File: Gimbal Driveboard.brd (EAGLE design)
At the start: 68.6 x 58.7 mm, 23 parts, among them J2 APP_2POS_CONFIG12V_HORIZ, U1 OKI-78SR-5/1.5-W36HC, U2 MAX232D, U3 MAX232D

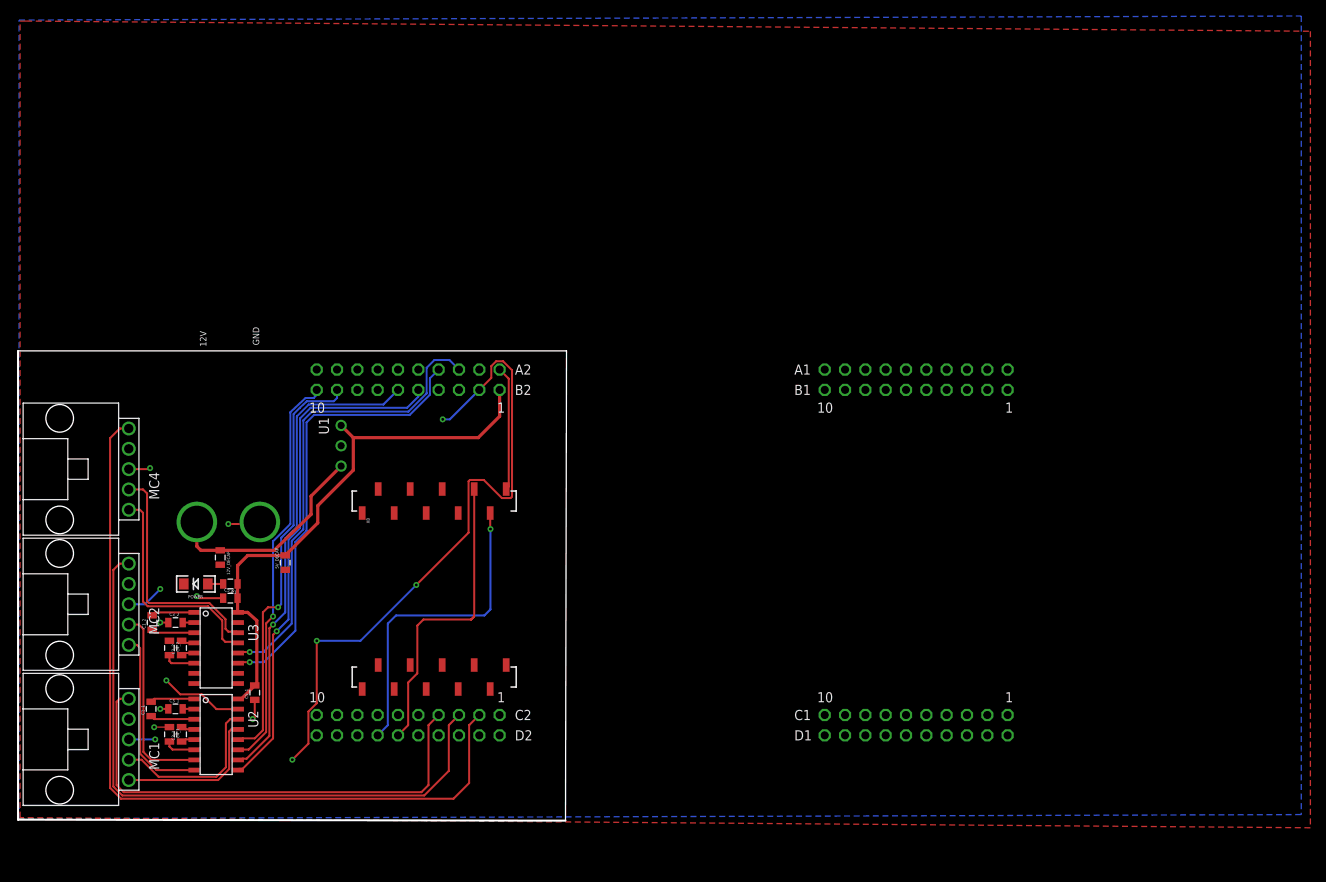
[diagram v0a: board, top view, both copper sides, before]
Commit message: Remade schematic to avoid physical interference with ethernet port
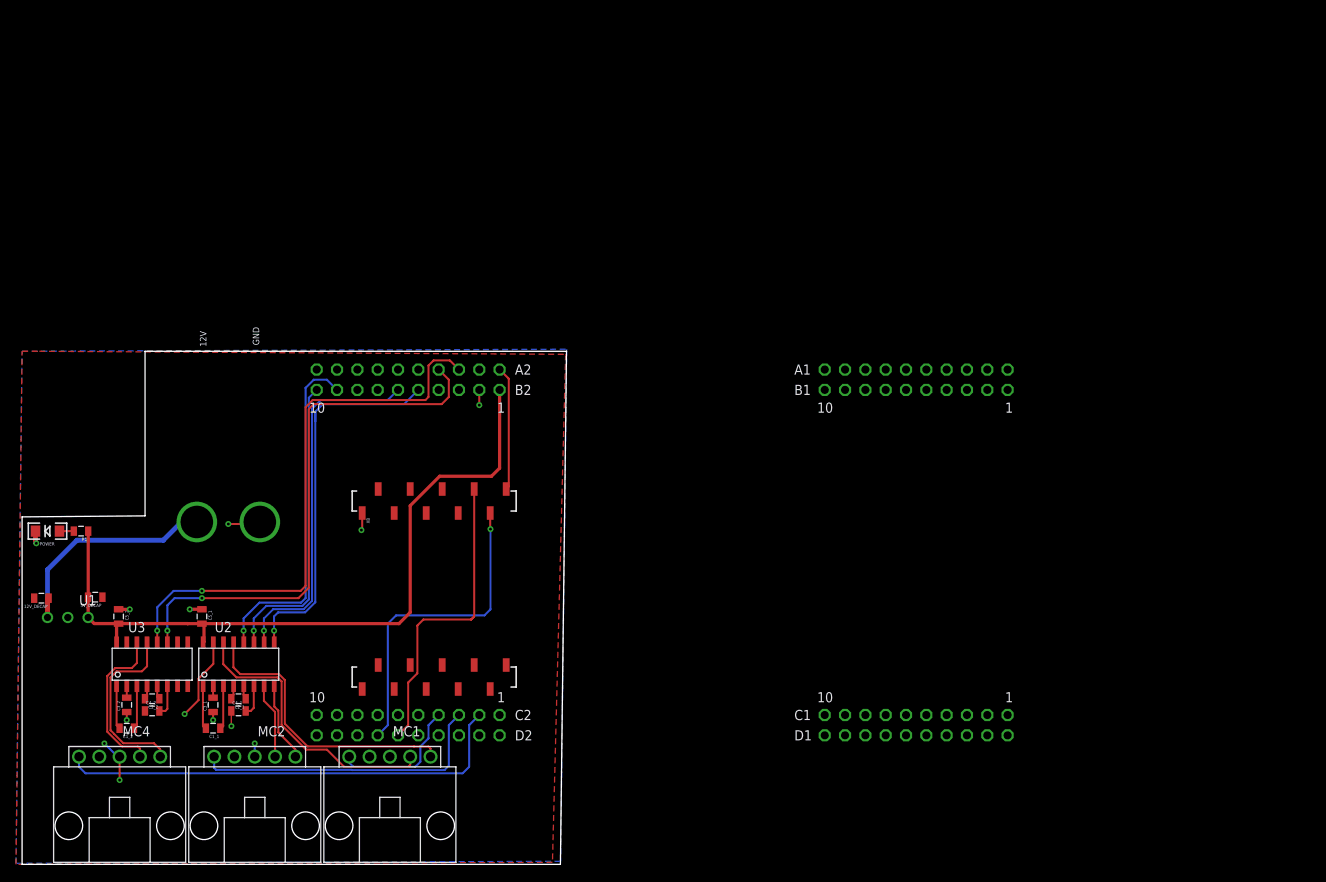
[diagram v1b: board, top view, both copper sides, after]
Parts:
- moved U1 41.3 mm to (3.68, 25.3), turned to 180 degrees
- moved MC4 36.0 mm to (12.7, 7.87), turned to 180 degrees
- moved MC1 32.7 mm to (46.5, 7.87), turned to 180 degrees
- moved MC2 24.7 mm to (29.6, 7.87), turned to 180 degrees
- moved 5V_DECAP 24.1 mm to (9.65, 27.8), turned to 180 degrees
- moved 12V_DECAP 22.9 mm to (2.92, 27.7), turned to 180 degrees
- moved R1 19.8 mm to (7.87, 36.1)
- moved POWER 19.7 mm to (3.68, 36.1)
- moved C5_2 14.2 mm to (12.6, 25.4), turned to 270 degrees
- moved C1_2 13.6 mm to (13.6, 11.4), turned to 180 degrees
- moved C3_2 12.0 mm to (13.6, 14.4), turned to 90 degrees
- moved C5_1 11.6 mm to (23.0, 25.4), turned to 270 degrees
- moved U2 9.23 mm to (27.6, 19.4), turned to 0 degrees
- moved C4_1 9.12 mm to (27.6, 13.6), turned to 0 degrees
- moved C2_1 8.39 mm to (27.6, 15.1), turned to 180 degrees
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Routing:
- net GND: track 117.5 -> 34.1 mm, vias 14 -> 13
- net PWM_1: track 61.1 -> 16.9 mm
- net PWM_3: track 101.8 -> 57.7 mm
- net PWM_2: track 80.5 -> 37.9 mm
- net +5V: track 70.2 -> 94.1 mm
- net N$37: track 19.0 -> 36.2 mm
- net RX_2: track 64.9 -> 48.9 mm
- net N$36: track 20.7 -> 35.7 mm
- net N$35: track 24.8 -> 9.97 mm
- net TX_2: track 60.6 -> 45.9 mm
- net TX_1: track 50.5 -> 37.5 mm
- net N$34: track 22.4 -> 9.95 mm
- net TX_3: track 55.9 -> 67.7 mm, vias 1 -> 2
- net RX_3: track 59.3 -> 70.8 mm, vias 1 -> 2
- net N$32: track 29.6 -> 19.9 mm
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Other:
- board size 68.6 x 58.7 mm -> 68.1 x 64.1 mm

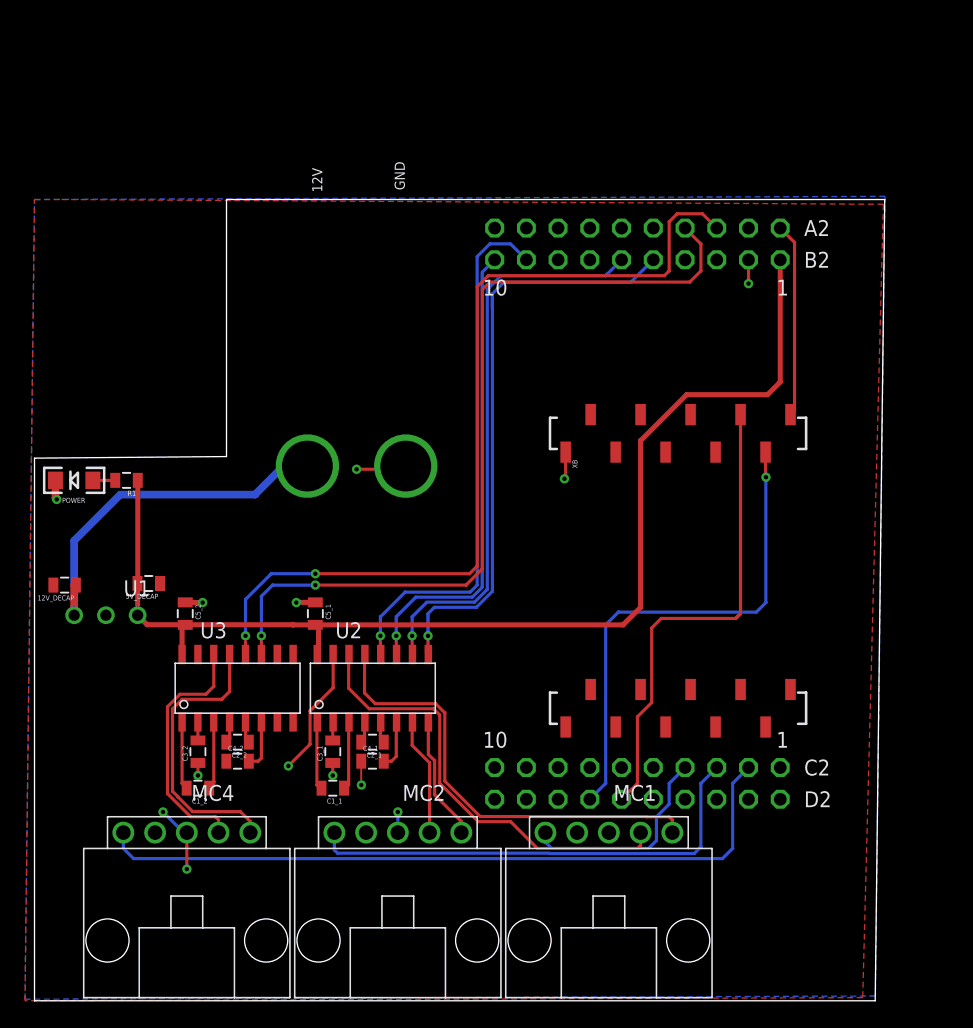
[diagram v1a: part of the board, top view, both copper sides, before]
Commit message: Updated schematic and board for final board review
added I2C Molex SL4
Added mounting tab and holes
cleaned up lines and traces
Added signature and board information
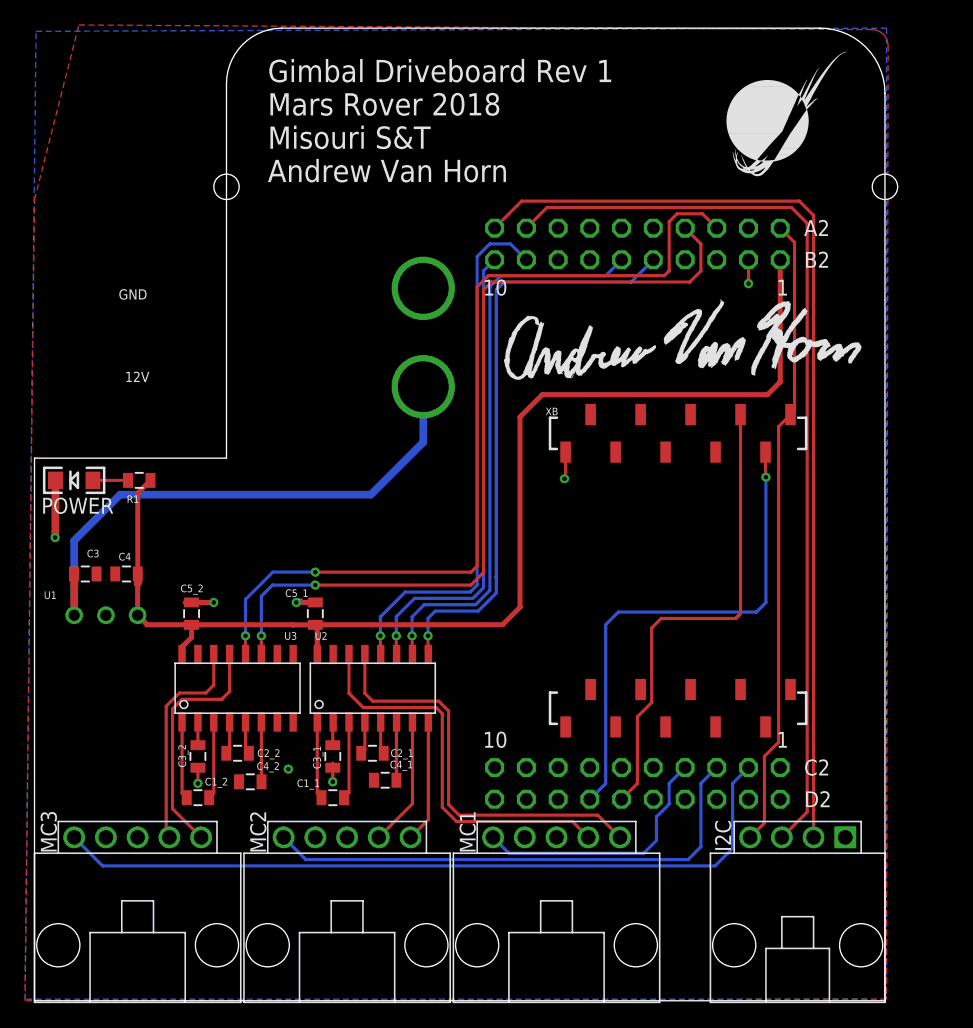
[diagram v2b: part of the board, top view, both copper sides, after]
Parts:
- removed 12V_DECAP, 5V_DECAP: 10uF, SparkFun-Capacitors:0805
- removed MC4: SL05, MRDT-Connectors:MOLEX_SL_05_TH
- added C3, C4: 10uF, SparkFun-Capacitors:0805
- added I2C: SL04, MRDT-Connectors:MOLEX_SL_04_TH
- added LOGO1: MRDT_LOGO, MRDT-Hardware:MRDT_LOGO
- added MC3: SL05, MRDT-Connectors:MOLEX_SL_05_TH
- added U$3: ANDREW_VAN_HORN_SIGNATURE, MRDT-Signatures:ANDREW_VAN_HORN_SIGNATURE
- moved J2 29.8 mm to (3.43, 39.6), turned to 0 degrees
- moved MC1 4.21 mm to (42.3, 7.49)
- moved MC2 4.08 mm to (25.5, 7.49)
- moved C4_2 1.94 mm to (17.8, 11.9)
- moved C4_1 1.83 mm to (28.6, 12.1)
- moved R1 1.02 mm to (8.89, 36.1)
- moved C2_1 0.89 mm to (27.6, 14.2)
- moved C2_2 0.89 mm to (16.8, 14.2)
- moved C1_1 0.76 mm to (24.4, 10.7)
- moved C1_2 0.76 mm to (13.6, 10.7)
- moved C5_2 0.51 mm to (13.1, 25.4)
- moved C3_1 0.38 mm to (24.4, 14.0)
- moved C3_2 0.38 mm to (13.6, 14.0)
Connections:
- new net SCL: I2C.3, U$1.PN5
- new net SDA: I2C.2, U$1.PN4
- net +3V3: now also I2C.4
- net +5V: now also C4.2; no longer 5V_DECAP.2
- net GND: now also C3.2, C4.1, I2C.1, MC3.3; no longer 12V_DECAP.2, 5V_DECAP.1, MC4.3
- net N$32: now also MC3.4; no longer MC4.4
- net N$33: now also MC3.5; no longer MC4.5
- net N$5: now also C3.1; no longer 12V_DECAP.1
- net PWM_3: now also MC3.1; no longer MC4.1
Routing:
- net SDA: track 0.00 -> 76.7 mm
- net SCL: track 0.00 -> 73.7 mm
- net +3V3: track 15.5 -> 50.7 mm
- net GND: track 34.1 -> 15.7 mm, vias 13 -> 8
- net N$5: track 29.7 -> 44.9 mm
- net N$36: track 35.7 -> 31.4 mm
- net PWM_1: track 16.9 -> 20.8 mm
- net PWM_3: track 57.7 -> 61.2 mm
- net PWM_2: track 37.9 -> 41.4 mm
- net N$33: track 22.8 -> 19.3 mm
- net N$37: track 36.2 -> 32.7 mm
- net +5V: track 94.1 -> 96.7 mm
- net N$32: track 19.9 -> 17.6 mm
- net RX_2: track 48.9 -> 47.8 mm
- net N$17: track 1.79 -> 2.81 mm
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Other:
- board size 68.1 x 64.1 mm -> 68.1 x 77.9 mm
- board text added: "Gimbal Driveboard Rev 1 Mars Rover 2018 Misouri S&T Andrew Van Horn"

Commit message: Final board review and Rev 1 Gerbs
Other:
- board size 68.1 x 77.9 mm -> 68.1 x 82.9 mm
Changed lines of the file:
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@@
 <plain>
 <wire x1="0.508" y1="-5.588" x2="68.58" y2="-5.588" width="0" layer="20"/>
-<wire x1="68.58" y1="-5.588" x2="68.58" y2="67.05973125" width="0" layer="20"/>
-<wire x1="68.58" y1="67.05973125" x2="63.37673125" y2="72.263" width="0" layer="20" curve="90"/>
-<wire x1="63.37673125" y1="72.263" x2="20.32" y2="72.263" width="0" layer="20"/>
-<wire x1="20.32" y1="72.263" x2="15.875" y2="67.818" width="0" layer="20" curve="90"/>
-<wire x1="15.875" y1="67.818" x2="15.875" y2="37.846" width="0" layer="20"/>
+<wire x1="68.58" y1="-5.588" x2="68.58" y2="66.560715625" width="0" layer="20"/>
+<wire x1="68.58" y1="66.560715625" x2="57.797715625" y2="77.343" width="0" layer="20" curve="90"/>
+<wire x1="57.797715625" y1="77.343" x2="24.108775" y2="77.343" width="0" layer="20"/>
+<wire x1="24.108775" y1="77.343" x2="15.875" y2="69.109225" width="0" layer="20" curve="90"/>
+<wire x1="15.875" y1="69.109225" x2="15.875" y2="37.846" width="0" layer="20"/>
 <wire x1="15.875" y1="37.846" x2="0.508" y2="37.846" width="0" layer="20"/>
 <wire x1="0.508" y1="37.846" x2="0.508" y2="-5.588" width="0" layer="20"/>
-<hole x="15.875" y="59.563" drill="2.032"/>
-<hole x="68.58" y="59.563" drill="2.032"/>
+<hole x="15.875" y="64.643" drill="2.032"/>
+<hole x="68.58" y="64.643" drill="2.032"/>
 <text x="19.177" y="59.944" size="1.778" layer="25">Gimbal Driveboard Rev 1
 Mars Rover 2018
@@
 <polygon width="0.254" layer="1">
 <vertex x="0.508" y="58.547"/>
-<vertex x="4.064" y="72.517"/>
-<vertex x="67.55731875" y="72.143509375" curve="-89.795916"/>
-<vertex x="68.831909375" y="70.858628125"/>
+<vertex x="3.175" y="78.105"/>
+<vertex x="67.945" y="77.724"/>
 <vertex x="68.707" y="-5.461"/>
 <vertex x="-0.254" y="-5.588"/>
@@
 <via x="24.384" y="11.938" extent="1-16" drill="0.35"/>
 <polygon width="0.254" layer="16">
-<vertex x="0.635" y="72.009"/>
-<vertex x="68.707" y="72.263"/>
+<vertex x="0.127" y="77.851"/>
+<vertex x="68.199" y="78.105"/>
 <vertex x="68.707" y="-5.461"/>
 <vertex x="-0.254" y="-5.461"/>

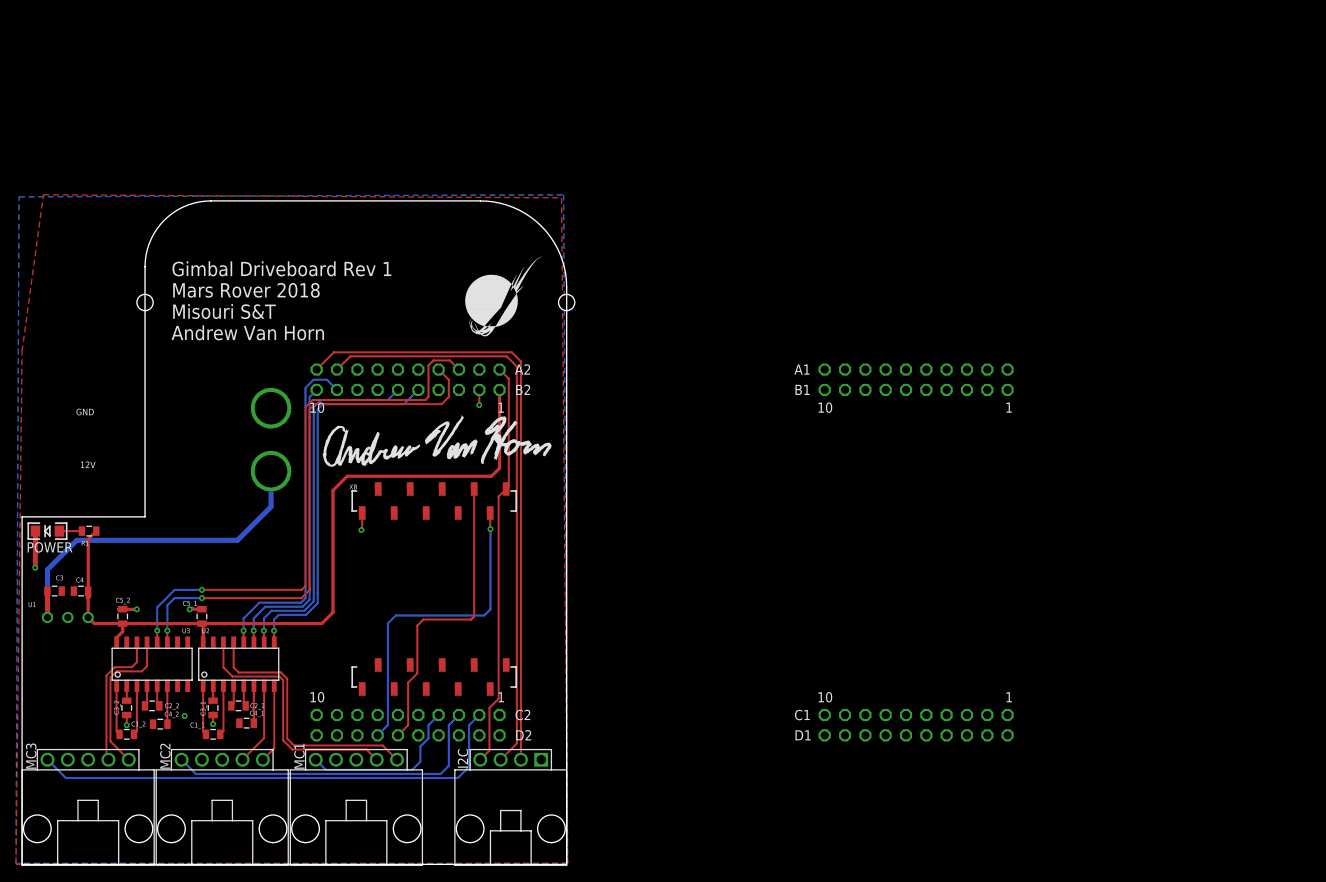
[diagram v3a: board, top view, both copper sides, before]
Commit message: removed TIVA holes on outside of board and rotated silkscreen
I replaced the TIVA package with just the ehaders and re-assigned all the pins in the schematic to match the physical layout on the old package. I rotated the silkscreen 180 so it is oriented right when it is mounted to rover.
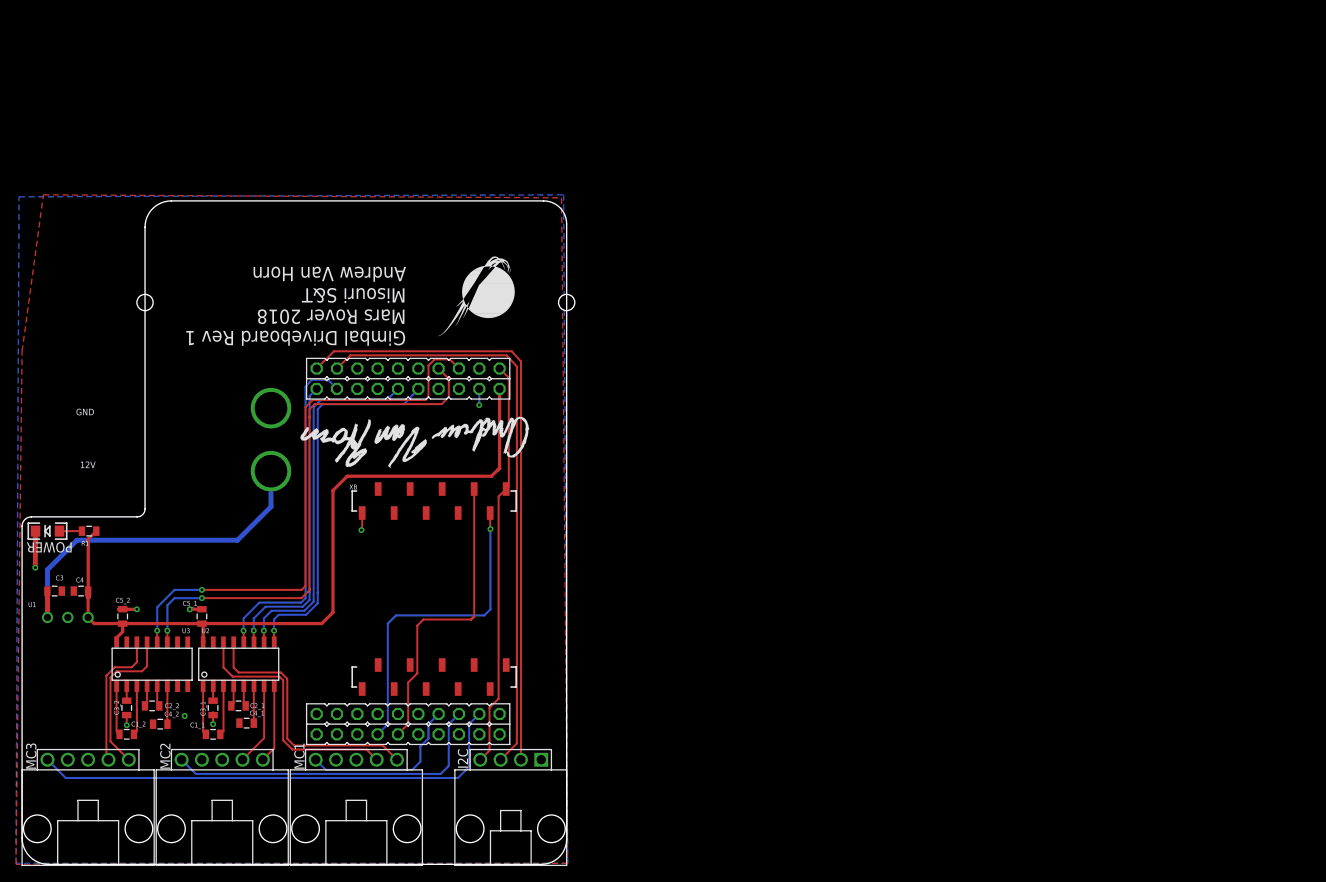
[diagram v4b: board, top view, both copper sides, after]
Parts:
- removed U$1: TIVA-1294, MRDT-Microcontrollers:TIVA-C-CONNECTED
- added U$2: TI_BACKPACK_HEADER, TI_HEADERS:TI_BACKPACK_HEADER
- moved U$3 29.5 mm to (65.2, 51.3), turned to 180 degrees
- moved LOGO1 13.2 mm to (62.1, 71.2), turned to 180 degrees
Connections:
- net +3V3: now also U$2.10; no longer U$1.+3V3_1, U$1.+3V3_2
- net +5V: now also U$2.20; no longer U$1.+5V_1, U$1.+5V_2
- net GND: now also U$2.19; no longer U$1.GND_1, U$1.GND_2, U$1.GND_3, U$1.GND_4
- net PWM_1: now also U$2.27; no longer U$1.PM0
- net PWM_2: now also U$2.28; no longer U$1.PK5
- net PWM_3: now also U$2.29; no longer U$1.PK4
- net RX_1: now also U$2.12; no longer U$1.PA4
- net RX_2: now also U$2.16; no longer U$1.PK0
- net RX_3: now also U$2.8; no longer U$1.PP0
- net SCL: now also U$2.2; no longer U$1.PN5
- net SDA: now also U$2.1; no longer U$1.PN4
- net TX_1: now also U$2.11; no longer U$1.PA5
- net TX_2: now also U$2.15; no longer U$1.PK1
- net TX_3: now also U$2.7; no longer U$1.PP1
- net XB_RX: now also U$2.34; no longer U$1.PQ3/PA2
- net XB_TX: now also U$2.35; no longer U$1.PQ2/PA3
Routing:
- net +5V: track 96.7 -> 97.6 mm
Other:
- outline, holes or cut-outs redrawn
